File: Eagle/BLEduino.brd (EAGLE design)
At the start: 40 x 23.4 mm, 90 parts, among them Q1 BSS138, Q2 BSS138, Q3 BSS138, T1 FDN340P/PMV48XP, T2 PMV48XP, U1 ATMEGA32U4-XUMU, U2 NCP1117-5, U3 ATMEGA8/168/328MLF, U4 LP2985-33DBVR, X1 USB-MICROB, Y2 16MHz, Y3 16MHz KX-7, Y4 16MHz

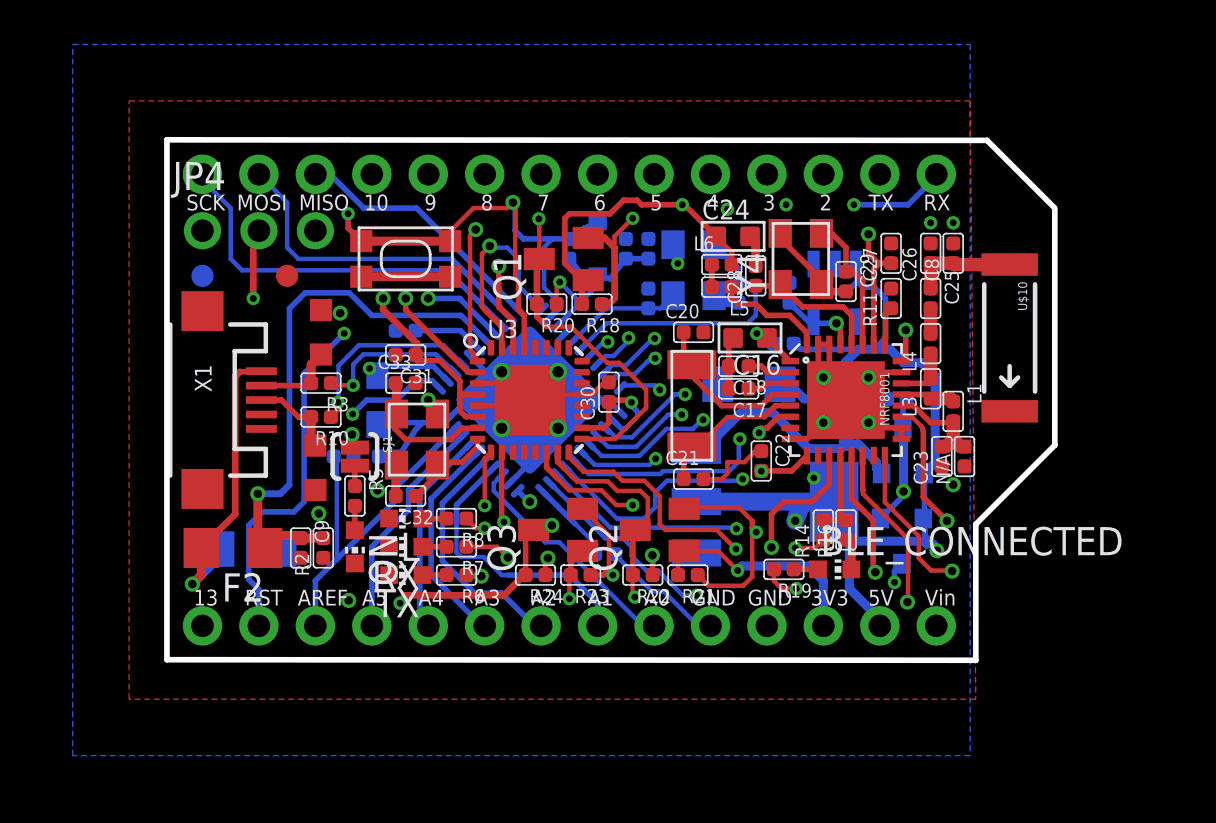
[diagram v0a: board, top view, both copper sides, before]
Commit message: Updated design files and BOM with the latest 6-layered board
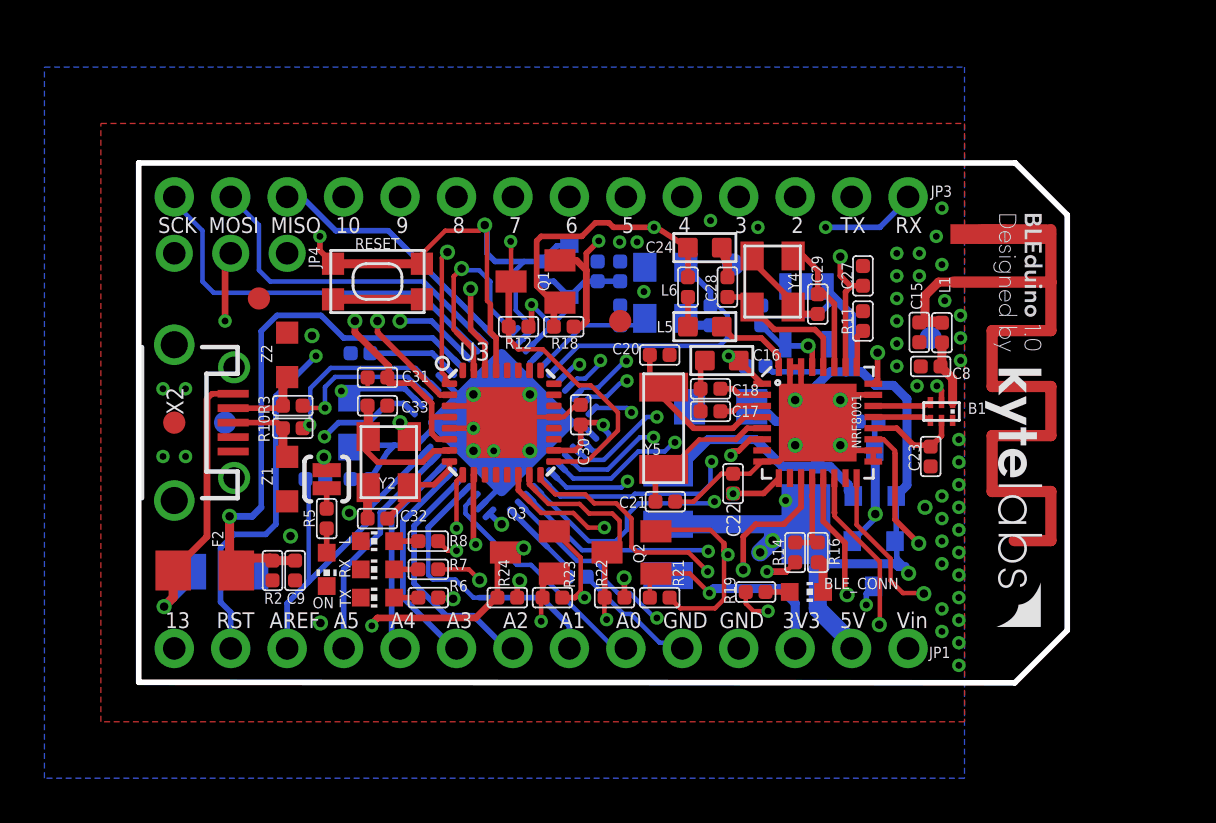
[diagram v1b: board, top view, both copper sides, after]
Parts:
- removed 32.768KHZ: FITNESSDEVICE_CRYSTAL-ABS10, bluetooth:FITNESSDEVICE_CRYSTAL-ABS10
- removed BLE_CONNECTED: blue, adafruit:CHIP-LED0603
- removed C25: 1.8pF, Discrete:C0402
- removed C26: 1.2pF, Discrete:C0402
- removed L3: 8.2nH, Discrete:L0402
- removed L4: 3.9nH, Discrete:L0402
- removed N/A: 0, Discrete:C0402
- removed R20: 10K, Discrete:R0402
- removed U$10: ANTENNA2SMD5, SparkFun:ANTENNA-CHIP5
- removed X1: USB-MICROB, SparkFun:USB-MICROB
- added ANT1: ANTENNA, adafruit:RN-ANT
- added B1: BALUN0603, SparkFun:BALUN-0603
- added BLE_CONN: blue, adafruit:CHIP-LED0603
- added C15: n/a, Discrete:C0402
- added R12: 10K, Discrete:R0402
- added SILK_1: (no value), Custom:V3_KYTELABS_TOP
- added SILK_2: (no value), Custom:V3_MAKESIMPLY_BOTTOM
- added U$1: (no value), SparkFun:OSHW-LOGO-S
- added U$12, U$27: FIDUCIAL, adafruit:FIDUCIAL_1MM
- added U$28, U$29: FIDUCIAL1X2, SparkFun:FIDUCIAL-1X2
- added X2: SPARKFUN_USB-MICROB, Micro_USB:SPARKFUN_USB-MICROB
- added Y5: Y5, bluetooth:FITNESSDEVICE_CRYSTAL-ABS10
- C8: value 1.5pF -> n/a
- L1: value 5.6nH -> n/a
- L5: device Discrete:L0402 -> Discrete:L0603
- moved U$53 32.9 mm to (40.1, 20.1)
- moved C8 5.19 mm to (40.1, 18.8), turned to 180 degrees
- moved L1 3.58 mm to (40.6, 20.3), turned to 90 degrees
- moved C5 2.27 mm to (14.5, 19.4)
- moved L5 1.93 mm to (30.0, 20.6)
- moved Z2 1.83 mm to (11.2, 19.3)
- moved L6 1.83 mm to (29.2, 22.4), turned to 90 degrees
- moved C20 1.83 mm to (27.9, 19.3)
- moved C29 1.63 mm to (35.1, 21.6)
- moved C1 1.63 mm to (35.1, 14.7)
- moved R16 1.63 mm to (35.1, 10.4)
- moved T1 1.63 mm to (37.6, 9.91)
- moved T2 1.63 mm to (37.6, 14.0)
- moved C32 1.63 mm to (15.2, 11.9)
- moved C9 1.63 mm to (10.5, 9.60)
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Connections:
- removed net N$27: C25.1, C26.1, C8.1, U$10.FEED
- new net N$9: ANT1.FEED, C15.1, L1.2
- net +5V: now also R12.1; no longer R20.1
- net BLE_SCK: now also R12.2; no longer R20.2
- net D+: now also X2.D+; no longer X1.D+
- net D-: now also X2.D-; no longer X1.D-
- net GND: now also ANT1.GND, B1.2, BLE_CONN.C, C15.2, X2.GND; no longer BLE_CONNECTED.C, C26.2, N/A.1, X1.GND
- net N$19: now also Y5.P$1; no longer 32.768KHZ.P$1
- net N$20: now also Y5.P$2; no longer 32.768KHZ.P$2
- net N$23: now also B1.5; no longer L1.2, N/A.2
- net N$24: now also B1.3; no longer L3.2, L4.1
- net N$25: now also B1.4; no longer L1.1, L3.1
- net N$26: now also B1.1, C8.1, L1.1; no longer C25.2, L4.2
- net N$8: now also BLE_CONN.A; no longer BLE_CONNECTED.A
- net VUSBD: now also X2.VBUS; no longer X1.VBUS
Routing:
- net N$27: track 4.73 -> 0.00 mm
- net N$9: track 0.00 -> 4.48 mm
- net GND: track 73.0 -> 75.5 mm, vias 19 -> 63
- net BLE_SCK_SHIFTED: track 33.0 -> 30.7 mm
- net BLE_RESET: track 48.8 -> 46.8 mm
- net N$26: track 1.14 -> 2.96 mm
- net N$15: track 5.03 -> 3.63 mm
- net VUSB: track 61.1 -> 60.1 mm
- net IO13*: track 36.7 -> 35.7 mm
- net UCAP: track 3.16 -> 3.92 mm
- net BLE_RDNY: track 44.9 -> 44.2 mm
- net +5V: track 83.5 -> 83.7 mm, vias 11 -> 12
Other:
- board size 40 x 23.4 mm -> 41.8 x 23.4 mm
- board text added: "+"
- board text added: "JP1"
- board text added: "JP3"
- board text added: "RESET"
- board text added: "Y5"

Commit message: Final BLEduino Hardware Files
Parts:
- removed SILK_1: (no value), Custom:V3_KYTELABS_TOP
- added LOGO_TOP: (no value), Custom:V3_KYTELABS_TOP
- added R13: 10K, Discrete:R0402
- added R15: 20K, Discrete:R0402
- L: value green -> yellow
- ON: value red -> green
- moved R2 3.50 mm to (9.04, 12.1), turned to 180 degrees
- moved C9 2.07 mm to (9.04, 11.0), turned to 0 degrees
- moved C24 1.37 mm to (29.5, 22.9), turned to 90 degrees
- moved Z2 1.17 mm to (11.4, 18.2), turned to 0 degrees
- moved L6 1.02 mm to (28.2, 22.4)
- moved C29 0.92 mm to (35.6, 22.4)
- moved L5 0.76 mm to (30.7, 20.6)
- moved R6 0.51 mm to (17.5, 8.89)
- moved R7 0.51 mm to (17.5, 10.2)
- moved RX 0.51 mm to (15.2, 10.2)
- moved TX 0.51 mm to (15.2, 8.89)
- moved C32 0.51 mm to (15.2, 12.4)
- moved L 0.51 mm to (15.2, 11.4)
- moved R8 0.51 mm to (17.5, 11.4)
- moved C27 0.51 mm to (37.6, 22.9)
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- renumbered U$1 to LOGO_BOTTOM
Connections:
- new net BLE_RESET_SHIFTED: NRF8001.19, R13.2, R15.2
- net BLE_RESET: now also R13.1; no longer NRF8001.19
- net GND: now also R15.1, Y4.2, Y4.4; no longer Y4.1, Y4.3
- net N$29: now also Y4.3; no longer Y4.4
- net N$30: now also Y4.1; no longer Y4.2
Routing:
- net GND: track 75.5 -> 103.3 mm, vias 63 -> 62
- net BLE_RESET_SHIFTED: track 0.00 -> 3.88 mm
- net BLE_RESET: track 46.8 -> 43.0 mm
- net VUSB: track 60.1 -> 57.8 mm
- net 3V3: track 150.6 -> 152.9 mm
- net N$17: track 1.33 -> 2.81 mm
- net +5V: track 83.7 -> 82.5 mm
- net BLE_MISO_SHIFTED: track 28.7 -> 29.8 mm
- net RESET: track 51.3 -> 50.3 mm
- net VUSBD: track 14.3 -> 13.4 mm
- net N$15: track 3.63 -> 3.01 mm
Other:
- board text added: "-GND-"
- board text added: "3V"
- board text removed: "3V3"
- board text removed: "GND"

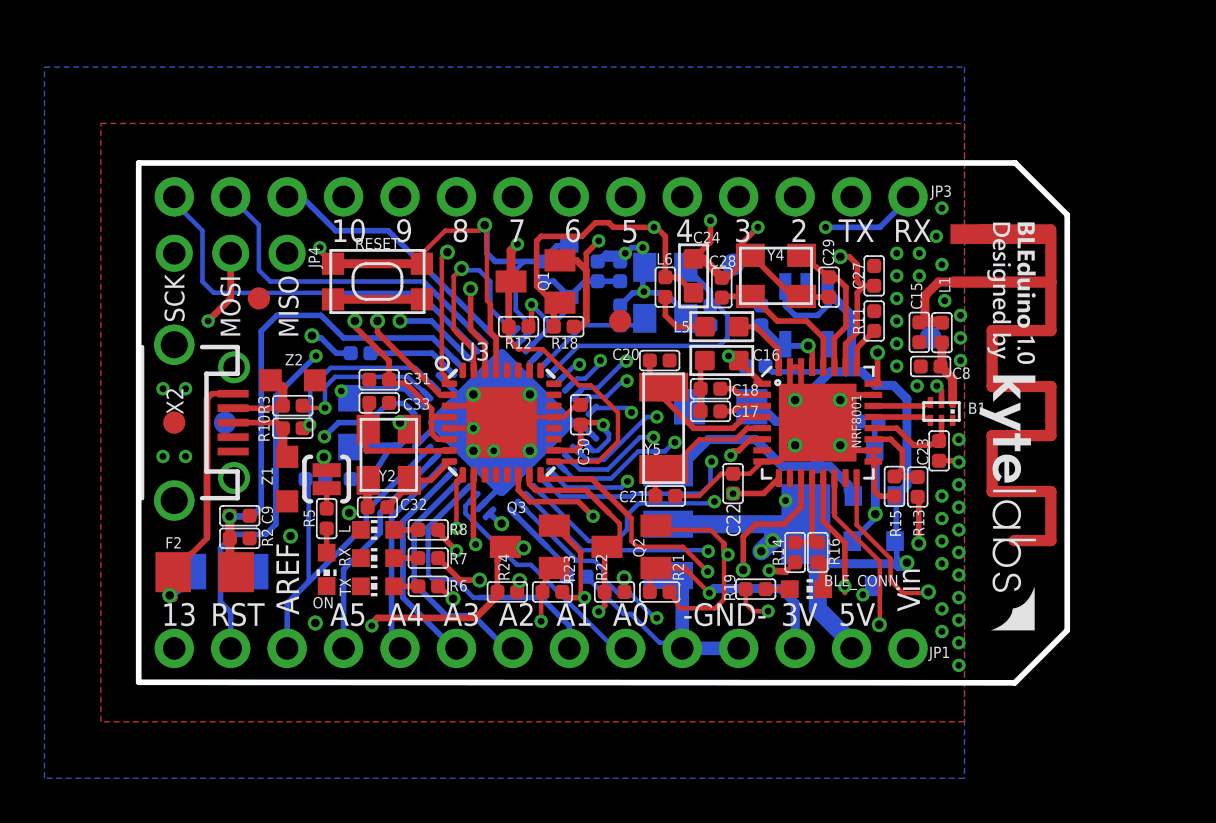
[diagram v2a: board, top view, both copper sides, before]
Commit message: Latest BLEduino Files
Should be the same as the BLEduino that will ship.
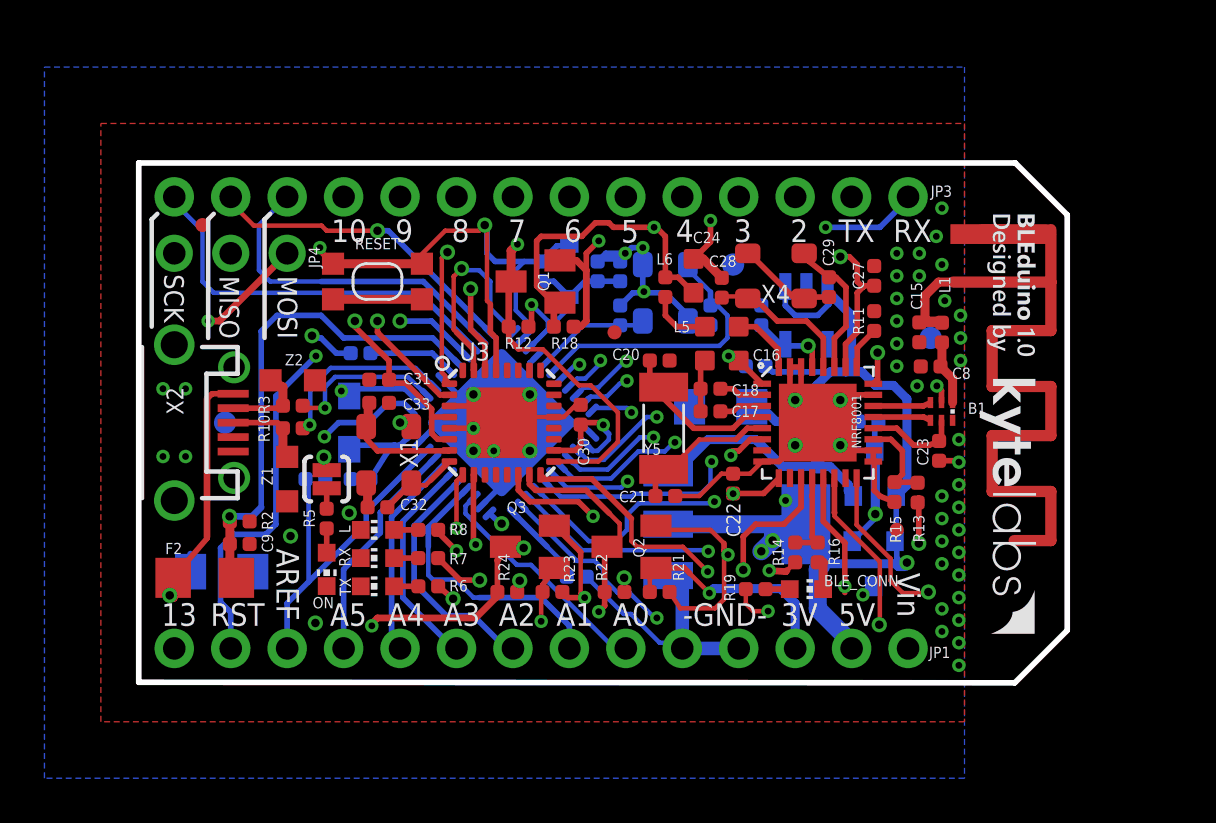
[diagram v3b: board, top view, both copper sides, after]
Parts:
- removed U$12, U$27, U$37: FIDUCIAL, adafruit:FIDUCIAL_1MM
- removed Y2, Y4: 16MHz, SmartPrj:CRYSTAL-3.2-2.5
- removed Y3: 16MHz KX-7, SmartPrj:CRYSTAL-3.2-2.5
- added JP2, JP5, JP6: FIDUCIALUFIDUCIAL, SparkFun:MICRO-FIDUCIAL
- added X1, X3, X4: (no value), Discrete:4P-SMD-3.2X2.5
- L2: device wuerth-elektronik:0805 -> Wuerth_Elektronik_eiSos_V6:0805
- moved LOGO_BOTTOM 0.51 mm to (43.9, 24.9)
- moved LOGO_TOP 0.36 mm to (42.9, 25.6)
- moved C9 0.25 mm to (9.04, 10.8)
- moved F2 0.25 mm to (7.47, 9.27)
- moved R13 0.25 mm to (39.5, 13.1)
- moved R15 0.25 mm to (38.5, 13.1)
- moved R2 0.25 mm to (9.04, 11.8)
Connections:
- net BLE_MISO: now also JP4.2; no longer JP4.3
- net BLE_MOSI: now also JP4.3; no longer JP4.2
- net GND: now also X1.1, X1.3, X3.1, X3.3, X4.1, X4.3; no longer Y2.2, Y2.4, Y3.2, Y3.4, Y4.2, Y4.4
- net MISO: now also JP3.2; no longer JP3.3
- net MOSI: now also JP3.3; no longer JP3.2
- net N$1: now also X1.4; no longer Y2.1
- net N$29: now also X4.4; no longer Y4.3
- net N$30: now also X4.2; no longer Y4.1
- net N$5: now also X1.2; no longer Y2.3
- net XTAL1: now also X3.2; no longer Y3.3
- net XTAL2: now also X3.4; no longer Y3.1
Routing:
- net GND: track 103.3 -> 99.8 mm, vias 62 -> 61
- net MISO: track 11.6 -> 14.3 mm, vias 0 -> 1
- net BLE_MOSI: track 47.3 -> 48.6 mm
- net N$5: track 4.48 -> 3.75 mm
- net VUSB: track 57.8 -> 57.2 mm
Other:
- board text added: "BLE SPI"
- board text added: "Main SPI"
